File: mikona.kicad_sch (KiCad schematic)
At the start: 0 parts

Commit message: Cleanup the project after moving to KiCad.
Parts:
- added F1: 8A, Fuse:Fuse_0603_1608Metric_Pad1.05x0.95mm_HandSolder, symbol Device:Fuse
- added JCAP1, JMAG1, JMAIN1: Molex 105429-1104, 1054291104:MOLEX_1054291104, symbol 1054291104:1054291104
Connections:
- new net: F1.1, JMAIN1.3
- new net +24V: F1.2
- new net +3.3V: JCAP1.3, JCAP1.4, JMAG1.3, JMAG1.4
- new net CAN_N: JMAIN1.2
- new net CAN_P: JMAIN1.1
- new net GND: JCAP1.1, JCAP1.2, JMAIN1.4
- new net MAGNET_A_2: JMAG1.1
- new net MAGNET_B_2: JMAG1.2
- no-connect marks 0 -> 6
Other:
- sheet Arm renamed Logic
- sheet Flyback renamed Power
- removed sheet IO
- removed sheet Kick
- sheet Logic ports: added CAN_N, CAN_P, CHARGE, DISCHARGE, DONE, KICK_A, KICK_B, SCL, SDA, VOUT_ADC; removed none
- sheet Power ports: added CHARGE, DISCHARGE, DONE, KICK_A, KICK_B, MAGNET_A_2, MAGNET_B_2, SCL, SDA, VOUT_ADC; removed none

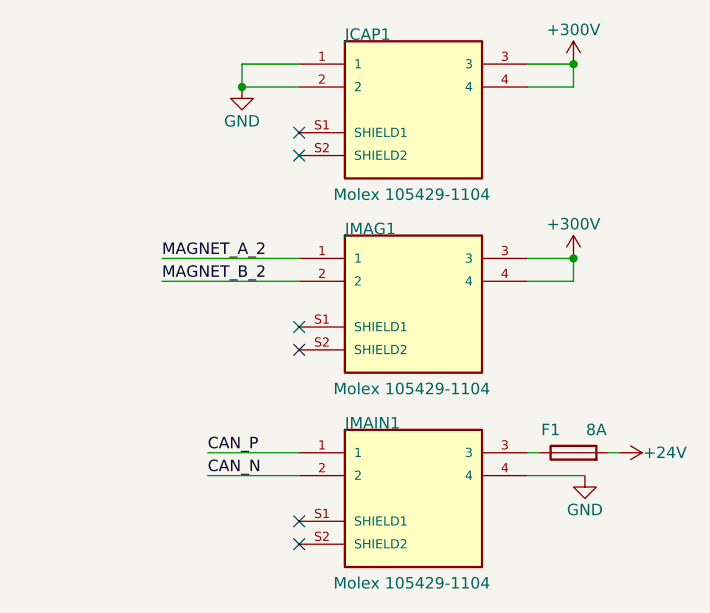
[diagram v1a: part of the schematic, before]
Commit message: Finish the layout, remove old routings, and setup internal planes.
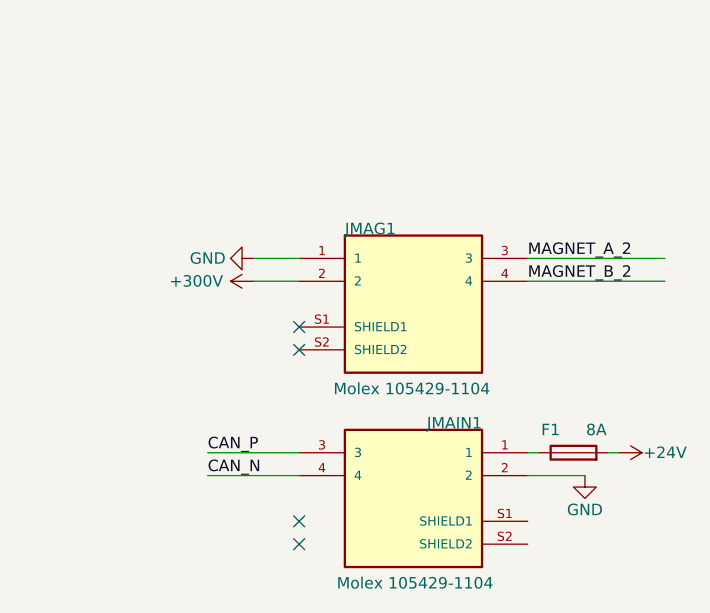
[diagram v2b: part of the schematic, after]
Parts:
- removed JCAP1: Molex 105429-1104, 1054291104:MOLEX_1054291104, symbol 1054291104:1054291104
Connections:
- net CAN_N: now also JMAIN1.4; no longer JMAIN1.2
- net CAN_P: now also JMAIN1.3; no longer JMAIN1.1
- net GND: now also JMAG1.1, JMAIN1.2; no longer JMAIN1.4
- net MAGNET_A_2: now also JMAG1.3; no longer JMAG1.1
- net MAGNET_B_2: now also JMAG1.4; no longer JMAG1.2
- net at F1.1: now also JMAIN1.1; no longer JMAIN1.3
- removed net +3.3V: JMAG1.3, JMAG1.4
- new net VDC: JMAG1.2
- no-connect marks 6 -> 4

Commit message: Finish the draft routing.
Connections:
- net CAN_N: now also JMAIN1.3; no longer JMAIN1.4
- net CAN_P: now also JMAIN1.4; no longer JMAIN1.3
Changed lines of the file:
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@@
     (stroke (width 0) (type default))
   )
-  (label "CAN_P" (at 195.58 125.73 0) (fields_autoplaced)
+  (label "CAN_P" (at 195.58 128.27 0) (fields_autoplaced)
     (effects (font (size 1.27 1.27)) (justify left bottom))
   )
@@
     (effects (font (size 1.27 1.27)) (justify left bottom))
   )
-  (label "CAN_N" (at 195.58 128.27 0) (fields_autoplaced)
+  (label "CAN_N" (at 195.58 125.73 0) (fields_autoplaced)
     (effects (font (size 1.27 1.27)) (justify left bottom))
   )

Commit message: Update MPNs and add jlcpcb comments.
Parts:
- F1: JLCPCB Comment (none) -> FUSE 8A; JLCPCB Footprint (none) -> 0603; MPN (none) -> SF-0603SA800M-2; Part SF-0603SA800M-2 -> (none)
- JMAG1, JMAIN1: LIFECYCLE STATUS Not Listed by Manufacturer -> (none); MANUFACTURER Molex -> (none); MANUFACTURER PART NUMBER 105429-1104 -> (none); MAXIMUM_PACKAGE_HEIGHT 11.16 mm -> (none); MPN (none) -> 1054291104; OCTOPART URL https://octopart.com/105429-1104-molex-97696459 -> (none); OCTOPARTID b40378db2bae6bc4 -> (none); PARTREV D -> (none); STANDARD Manufacturer Recommendations -> (none)
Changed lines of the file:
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@@
 (kicad_sch (version 20230121) (generator eeschema)
   (paper "A")
-  (no_connect (at 205.74 133.35))
+  (no_connect (at 231.14 133.35))
   (no_connect (at 205.74 114.3))
   (no_connect (at 205.74 111.76))
-  (no_connect (at 205.74 135.89))
+  (no_connect (at 231.14 135.89))
   (wire (pts (xy 96.52 97.79) (xy 110.49 97.79))
     (stroke (width 0) (type default))
@@
       (effects (font (size 1.27 1.27)) hide)
     )
-    (property "Part" "SF-0603SA800M-2" (at 236.22 125.73 90)
+    (property "MPN" "SF-0603SA800M-2" (at 236.22 125.73 0)
+      (effects (font (size 1.27 1.27)) hide)
+    )
+    (property "Description" "SF-0603SA800M-2" (at 236.22 125.73 0)
+      (effects (font (size 1.27 1.27)) hide)
+    )
+    (property "JLCPCB Comment" "FUSE 8A" (at 236.22 125.73 0)
+      (effects (font (size 1.27 1.27)) hide)
+    )
+    (property "JLCPCB Footprint" "0603" (at 236.22 125.73 0)
       (effects (font (size 1.27 1.27)) hide)
     )
@@
       (effects (font (size 1.27 1.27)) hide)
     )
-    (property "LIFECYCLE STATUS" "Not Listed by Manufacturer" (at 236.728 123.19 0)
-      (effects (font (size 1.27 1.27)) (justify left bottom) hide)
-    )
-    (property "OCTOPART URL" "https://octopart.com/105429-1104-molex-97696459" (at 236.728 123.19 0)
-      (effects (font (size 1.27 1.27)) (justify left bottom) hide)
-    )
-    (property "OCTOPARTID" "b40378db2bae6bc4" (at 236.728 123.19 0)
-      (effects (font (size 1.27 1.27)) (justify left bottom) hide)
-    )
-    (property "MANUFACTURER PART NUMBER" "105429-1104" (at 236.728 123.19 0)
-      (effects (font (size 1.27 1.27)) (justify left bottom) hide)
-    )
-    (property "PARTREV" "D" (at 218.44 130.81 0)
-      (effects (font (size 1.27 1.27)) (justify bottom) hide)
-    )
-    (property "MANUFACTURER" "Molex" (at 218.44 130.81 0)
-      (effects (font (size 1.27 1.27)) (justify bottom) hide)
-    )
-    (property "MAXIMUM_PACKAGE_HEIGHT" "11.16 mm" (at 218.44 130.81 0)
-      (effects (font (size 1.27 1.27)) (justify bottom) hide)
-    )
-    (property "STANDARD" "Manufacturer Recommendations" (at 218.44 130.81 0)
-      (effects (font (size 1.27 1.27)) (justify bottom) hide)
+    (property "MPN" "1054291104" (at 218.44 130.81 0)
+      (effects (font (size 1.27 1.27)) hide)
+    )
+    (property "Description" "1054291104" (at 218.44 130.81 0)
+      (effects (font (size 1.27 1.27)) hide)
+    )
+    (property "JLCPCB Comment" "" (at 218.44 130.81 0)
+      (effects (font (size 1.27 1.27)) hide)
+    )
+    (property "JLCPCB Footprint" "" (at 218.44 130.81 0)
+      (effects (font (size 1.27 1.27)) hide)
     )
     (pin "1")
@@
       (effects (font (size 1.27 1.27)) hide)
     )
-    (property "LIFECYCLE STATUS" "Not Listed by Manufacturer" (at 200.152 101.6 0)
-      (effects (font (size 1.27 1.27)) (justify left bottom) hide)
-    )
-    (property "OCTOPART URL" "https://octopart.com/105429-1104-molex-97696459" (at 200.152 101.6 0)
-      (effects (font (size 1.27 1.27)) (justify left bottom) hide)
-    )
-    (property "OCTOPARTID" "b40378db2bae6bc4" (at 200.152 101.6 0)
-      (effects (font (size 1.27 1.27)) (justify left bottom) hide)
-    )
-    (property "MANUFACTURER PART NUMBER" "105429-1104" (at 200.152 101.6 0)
-      (effects (font (size 1.27 1.27)) (justify left bottom) hide)
-    )
-    (property "PARTREV" "D" (at 218.44 109.22 0)
-      (effects (font (size 1.27 1.27)) (justify bottom) hide)
-    )
-    (property "MANUFACTURER" "Molex" (at 218.44 109.22 0)
-      (effects (font (size 1.27 1.27)) (justify bottom) hide)
-    )
-    (property "MAXIMUM_PACKAGE_HEIGHT" "11.16 mm" (at 218.44 109.22 0)
-      (effects (font (size 1.27 1.27)) (justify bottom) hide)
-    )
-    (property "STANDARD" "Manufacturer Recommendations" (at 218.44 109.22 0)
-      (effects (font (size 1.27 1.27)) (justify bottom) hide)
-    )
-    (pin "1")
+    (property "MPN" "1054291104" (at 218.44 109.22 0)
+      (effects (font (size 1.27 1.27)) hide)
+    )
+    (property "Description" "1054291104" (at 218.44 109.22 0)
+      (effects (font (size 1.27 1.27)) hide)
+    )
+    (property "JLCPCB Comment" "" (at 218.44 109.22 0)
+      (effects (font (size 1.27 1.27)) hide)
+    )
+    (property "JLCPCB Footprint" "" (at 218.44 109.22 0)
+      (effects (font (size 1.27 1.27)) hide)
+    )
+    (pin "1")

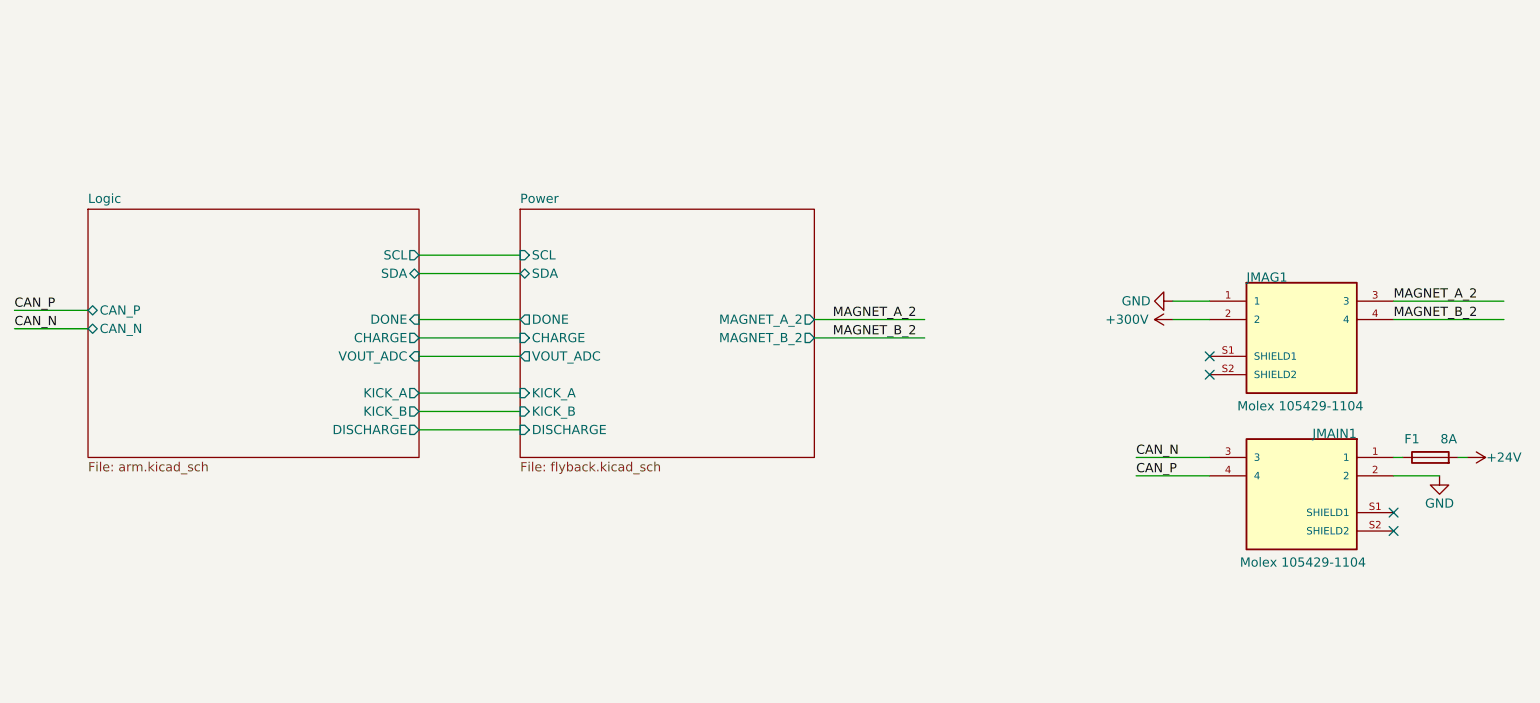
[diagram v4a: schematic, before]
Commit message: Move from stm32 to pic16 and remove other unnecessary parts.
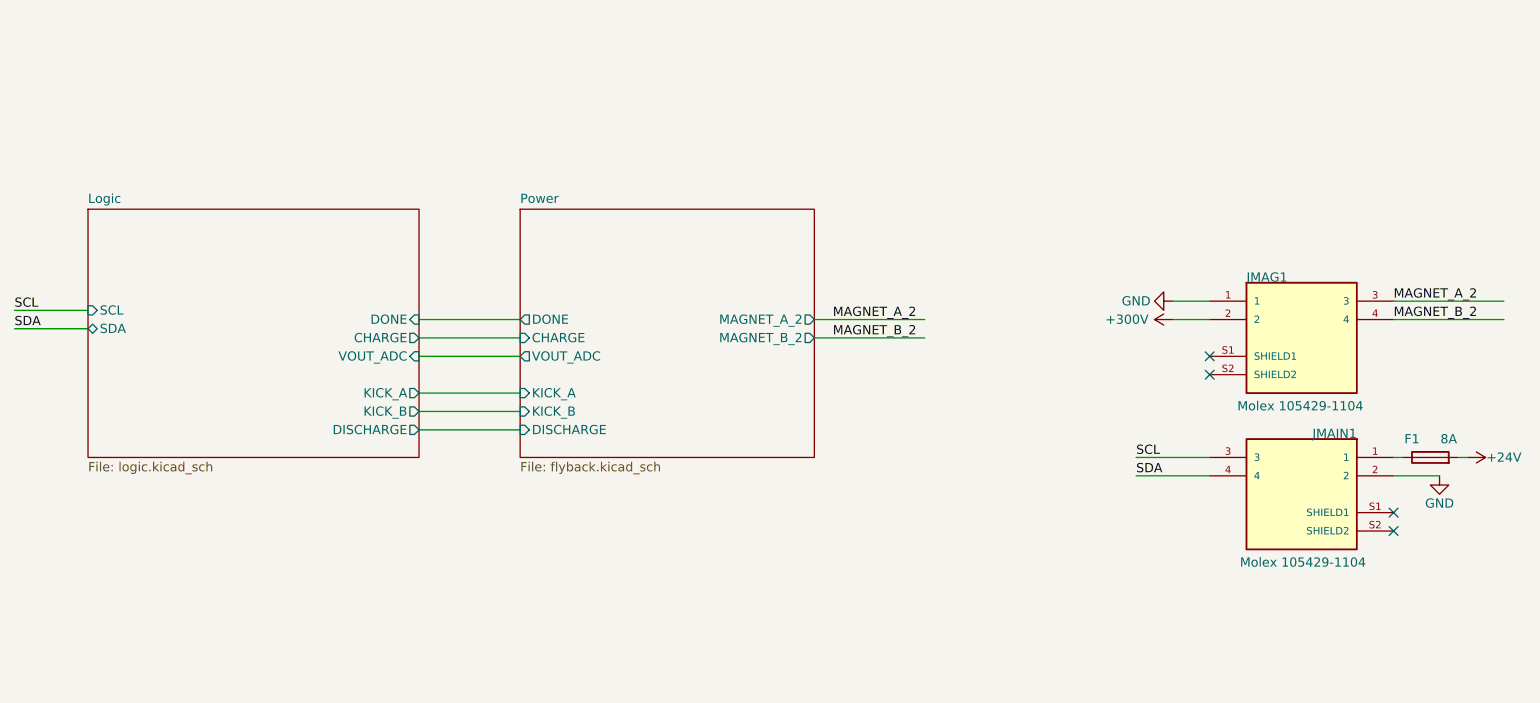
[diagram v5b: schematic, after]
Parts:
- F1: footprint Fuse:Fuse_0603_1608Metric_Pad1.05x0.95mm_HandSolder -> Fuse:Fuse_0603_1608Metric
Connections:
- net CAN_N renamed SCL
- net CAN_P renamed SDA
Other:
- sheet Logic: file arm.kicad_sch -> logic.kicad_sch
- sheet Logic ports: added none; removed CAN_N, CAN_P
- sheet Power ports: added none; removed SCL, SDA
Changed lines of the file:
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@@
   (no_connect (at 205.74 111.76))
   (no_connect (at 231.14 135.89))
-  (wire (pts (xy 96.52 97.79) (xy 110.49 97.79))
-    (stroke (width 0) (type default))
-  )
   (wire (pts (xy 40.64 107.95) (xy 50.8 107.95))
     (stroke (width 0) (type default))
@@
     (stroke (width 0) (type default))
   )
-  (wire (pts (xy 96.52 100.33) (xy 110.49 100.33))
-    (stroke (width 0) (type default))
-  )
   (wire (pts (xy 231.14 125.73) (xy 232.41 125.73))
     (stroke (width 0) (type default))
@@
     (stroke (width 0) (type default))
   )
-  (label "CAN_P" (at 195.58 128.27 0) (fields_autoplaced)
-    (effects (font (size 1.27 1.27)) (justify left bottom))
-  )
-  (label "CAN_N" (at 40.64 107.95 0) (fields_autoplaced)
+  (label "SDA" (at 195.58 128.27 0) (fields_autoplaced)
+    (effects (font (size 1.27 1.27)) (justify left bottom))
+  )
+  (label "SDA" (at 40.64 107.95 0) (fields_autoplaced)
     (effects (font (size 1.27 1.27)) (justify left bottom))
   )
@@
     (effects (font (size 1.27 1.27)) (justify left bottom))
   )
-  (label "CAN_P" (at 40.64 105.41 0) (fields_autoplaced)
-    (effects (font (size 1.27 1.27)) (justify left bottom))
-  )
-  (label "CAN_N" (at 195.58 125.73 0) (fields_autoplaced)
+  (label "SCL" (at 40.64 105.41 0) (fields_autoplaced)
+    (effects (font (size 1.27 1.27)) (justify left bottom))
+  )
+  (label "SCL" (at 195.58 125.73 0) (fields_autoplaced)
     (effects (font (size 1.27 1.27)) (justify left bottom))
   )
@@
       (effects (font (size 1.27 1.27)))
     )
-    (property "Footprint" "Fuse:Fuse_0603_1608Metric_Pad1.05x0.95mm_HandSolder" (at 236.22 127.508 90)
+    (property "Footprint" "Fuse:Fuse_0603_1608Metric" (at 236.22 127.508 90)
       (effects (font (size 1.27 1.27)) hide)
     )
@@
       (effects (font (size 1.27 1.27)) (justify left bottom))
     )
-    (property "Sheetfile" "arm.kicad_sch" (at 50.8 126.3146 0)
+    (property "Sheetfile" "logic.kicad_sch" (at 50.8 126.3146 0)
       (effects (font (size 1.27 1.27)) (justify left top))
     )
-    (pin "SDA" bidirectional (at 96.52 100.33 0)
-      (effects (font (size 1.27 1.27)) (justify right))
-    )
-    (pin "SCL" output (at 96.52 97.79 0)
-      (effects (font (size 1.27 1.27)) (justify right))
-    )
     (pin "KICK_A" output (at 96.52 116.84 0)
       (effects (font (size 1.27 1.27)) (justify right))
@@
       (effects (font (size 1.27 1.27)) (justify right))
     )
-    (pin "CAN_N" bidirectional (at 50.8 107.95 180)
+    (pin "SCL" input (at 50.8 105.41 180)
       (effects (font (size 1.27 1.27)) (justify left))
     )
-    (pin "CAN_P" bidirectional (at 50.8 105.41 180)
+    (pin "SDA" bidirectional (at 50.8 107.95 180)
       (effects (font (size 1.27 1.27)) (justify left))
     )
@@
       (effects (font (size 1.27 1.27)) (justify left top))
     )
-    (pin "SCL" input (at 110.49 97.79 180)
-      (effects (font (size 1.27 1.27)) (justify left))
-    )
-    (pin "SDA" bidirectional (at 110.49 100.33 180)
-      (effects (font (size 1.27 1.27)) (justify left))
-    )
     (pin "DONE" output (at 110.49 106.68 180)

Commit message: Change the parts that were not in stock.
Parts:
- F1: JLCPCB Comment FUSE 8A -> (none); JLCPCB Footprint 0603 -> (none)
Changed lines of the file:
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@@
-      (effects (font (size 1.27 1.27)) hide)
-    )
-    (property "JLCPCB Comment" "FUSE 8A" (at 236.22 125.73 0)
-      (effects (font (size 1.27 1.27)) hide)
-    )
-    (property "JLCPCB Footprint" "0603" (at 236.22 125.73 0)
       (effects (font (size 1.27 1.27)) hide)
     )
@@
     )
     (property "Description" "1054291104" (at 218.44 130.81 0)
-      (effects (font (size 1.27 1.27)) hide)
-    )
-    (property "JLCPCB Comment" "" (at 218.44 130.81 0)
-      (effects (font (size 1.27 1.27)) hide)
-    )
-    (property "JLCPCB Footprint" "" (at 218.44 130.81 0)
       (effects (font (size 1.27 1.27)) hide)
     )
@@
       (effects (font (size 1.27 1.27)) hide)
     )
-    (property "JLCPCB Comment" "" (at 218.44 109.22 0)
-      (effects (font (size 1.27 1.27)) hide)
-    )
-    (property "JLCPCB Footprint" "" (at 218.44 109.22 0)
-      (effects (font (size 1.27 1.27)) hide)
-    )
